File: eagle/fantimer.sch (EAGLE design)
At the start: 17 parts, among them IC1 PIC10F220, K1 PB2032-ND, Q1 2N7000-G, U1 IRM-01-5, X1 732-10957-ND

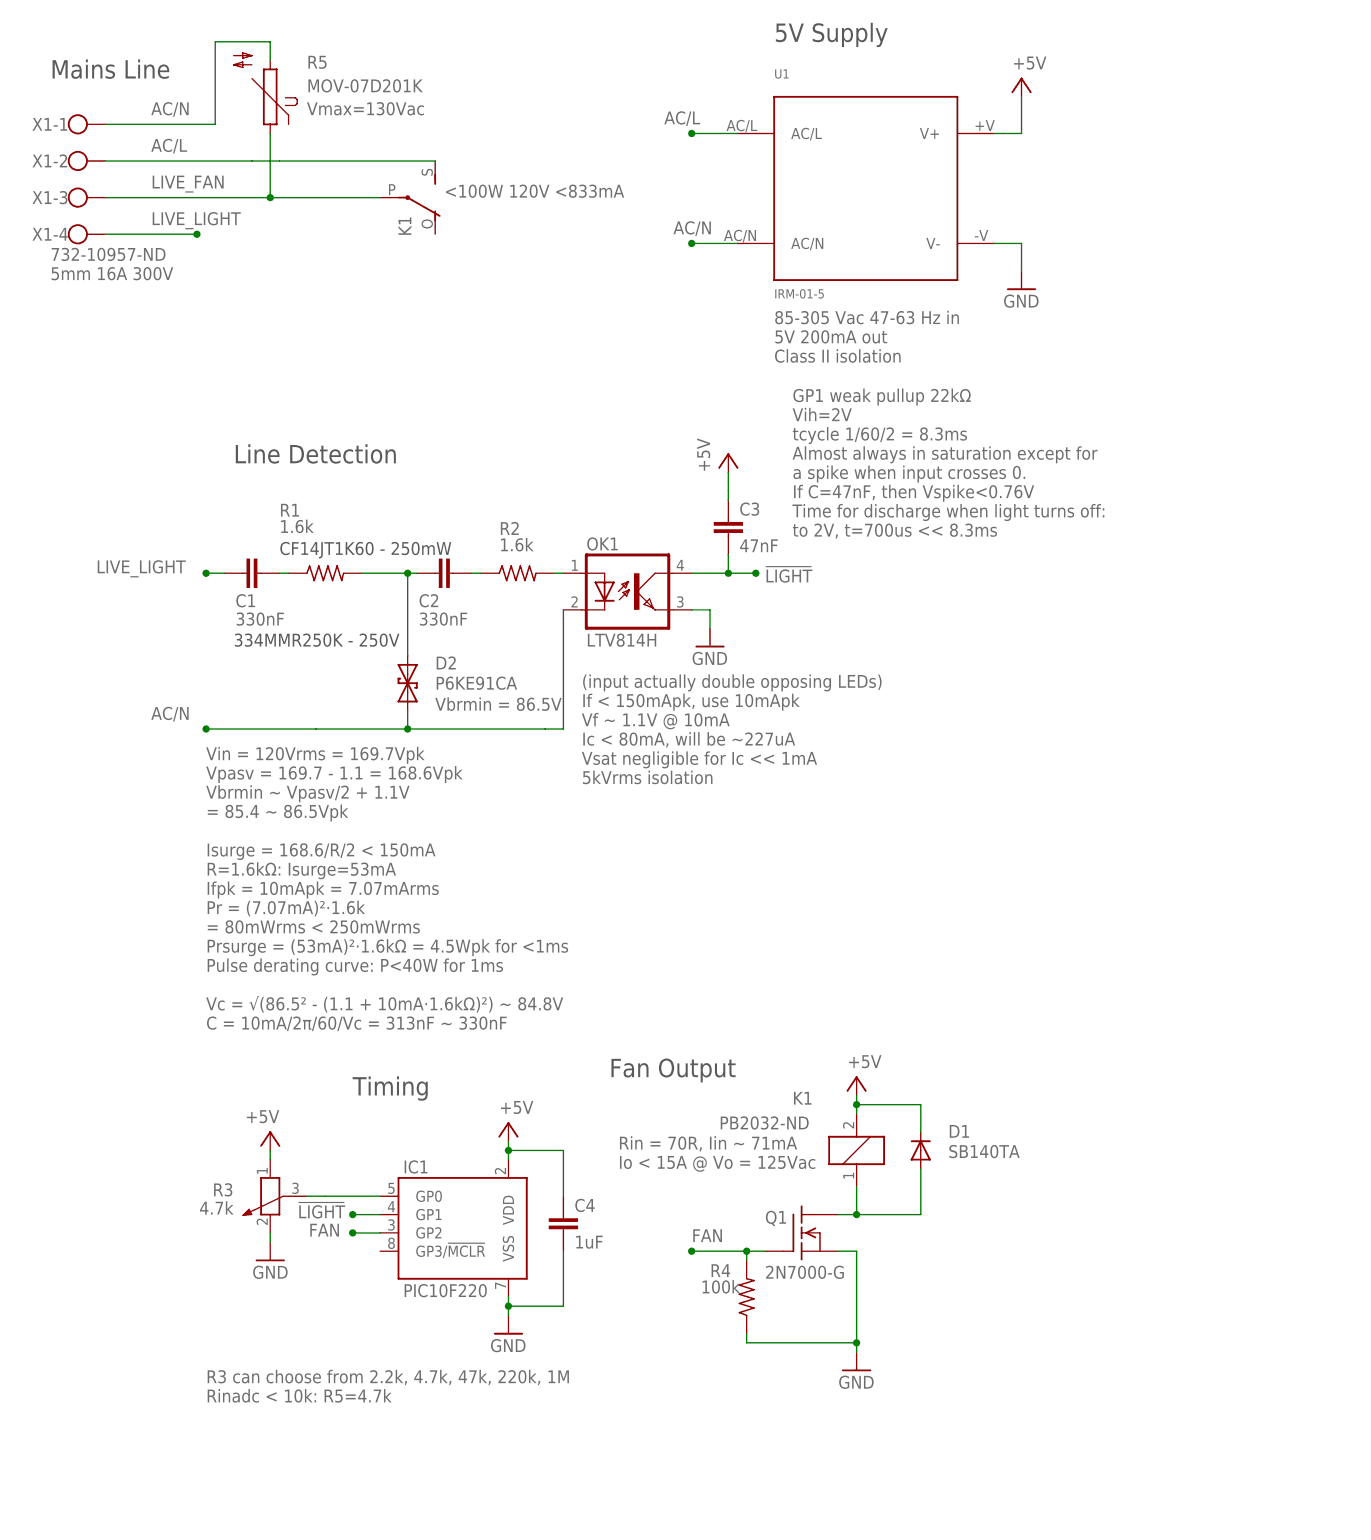
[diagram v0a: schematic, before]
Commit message: Increase detection filter cap; add pot cap
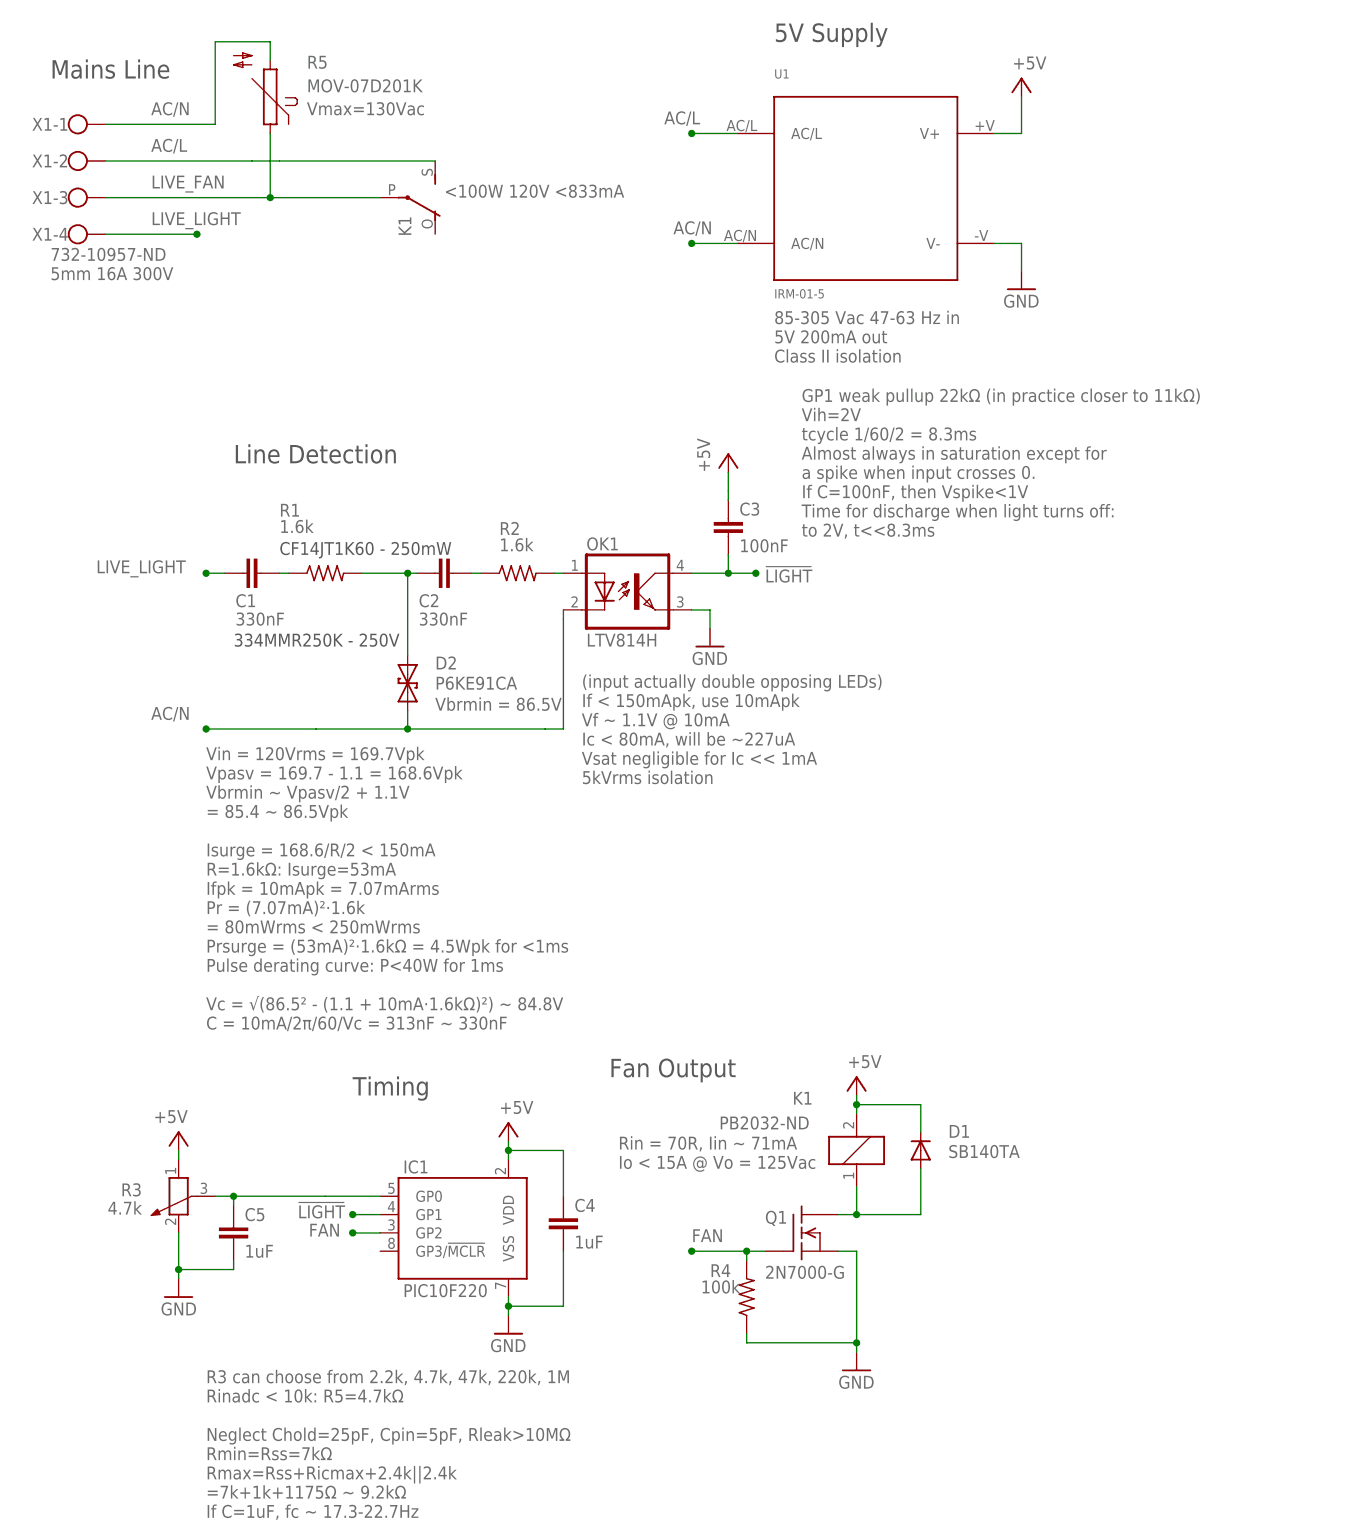
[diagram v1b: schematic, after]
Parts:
- added C5: 1uF, rcl:C-EU025-025X050
- C3: value 47nF -> 100nF
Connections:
- net ADJ: now also C5.1
- net GND: now also C5.2
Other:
- note added: "GP1 weak pullup 22kΩ (in practice closer to 11kΩ) Vih=2V tcycle 1/60/2 = 8.3ms Almost always in saturation except for a spike when input crosses 0. If C=100nF, then Vspike<1V Time for discharge when light turns off: to 2V, t<<8.3ms"
- note added: "R3 can choose from 2.2k, 4.7k, 47k, 220k, 1M Rinadc < 10k: R5=4.7kΩ Neglect Chold=25pF, Cpin=5pF, Rleak>10MΩ Rmin=Rss=7kΩ Rmax=Rss+Ricmax+2.4k||2.4k =7k+1k+1175Ω ~ 9.2kΩ If C=1uF, fc ~ 17.3-22.7Hz"
- note removed: "GP1 weak pullup 22kΩ Vih=2V tcycle 1/60/2 = 8.3ms Almost always in saturation except for a spike when input crosses 0. If C=47nF, then Vspike<0.76V Time for discharge when light turns off: to 2V, t=700us << 8.3ms"
- note removed: "R3 can choose from 2.2k, 4.7k, 47k, 220k, 1M Rinadc < 10k: R5=4.7k"
- moved on the sheet: R3
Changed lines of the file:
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@@
 <part name="P+6" library="supply1" library_urn="urn:adsk.eagle:library:371" deviceset="+5V" device=""/>
 <part name="GND5" library="supply1" library_urn="urn:adsk.eagle:library:371" deviceset="GND" device=""/>
-<part name="C3" library="rcl" library_urn="urn:adsk.eagle:library:334" deviceset="C-EU" device="025-025X050" package3d_urn="urn:adsk.eagle:package:23629/2" value="47nF"/>
+<part name="C3" library="rcl" library_urn="urn:adsk.eagle:library:334" deviceset="C-EU" device="025-025X050" package3d_urn="urn:adsk.eagle:package:23629/2" value="100nF"/>
 <part name="P+2" library="supply1" library_urn="urn:adsk.eagle:library:371" deviceset="+5V" device=""/>
 <part name="IC1" library="microchip-addl" deviceset="PIC10F220" device="-I/P" package3d_urn="urn:adsk.eagle:package:14440/1" value="PIC10F220"/>
@@
 <part name="C4" library="rcl" library_urn="urn:adsk.eagle:library:334" deviceset="C-EU" device="025-025X050" package3d_urn="urn:adsk.eagle:package:23629/2" value="1uF"/>
 <part name="R5" library="varistor" library_urn="urn:adsk.eagle:library:410" deviceset="S05K300" device="" package3d_urn="urn:adsk.eagle:package:30536/1" value="MOV-07D201K"/>
+<part name="C5" library="rcl" library_urn="urn:adsk.eagle:library:334" deviceset="C-EU" device="025-025X050" package3d_urn="urn:adsk.eagle:package:23629/2" value="1uF"/>
 </parts>
 <sheets>
@@
 <text x="-13.97" y="172.72" size="1.778" layer="96">5mm 16A 300V</text>
 <text x="7.62" y="21.59" size="1.778" layer="96" rot="MR180">R3 can choose from 2.2k, 4.7k, 47k, 220k, 1M
-Rinadc &lt; 10k: R5=4.7k</text>
+Rinadc &lt; 10k: R5=4.7kΩ
+Neglect Chold=25pF, Cpin=5pF, Rleak&gt;10MΩ
+Rmin=Rss=7kΩ
+Rmax=Rss+Ricmax+2.4k||2.4k
+=7k+1k+1175Ω ~ 9.2kΩ
+If C=1uF, fc ~ 17.3-22.7Hz</text>
 <text x="86.36" y="161.29" size="1.778" layer="96">85-305 Vac 47-63 Hz in
 5V 200mA out
@@
 C = 10mA/2π/60/Vc = 313nF ~ 330nF</text>
 <text x="39.37" y="113.03" size="1.778" layer="96">Vbrmin = 86.5V</text>
-<text x="88.9" y="137.16" size="1.778" layer="96">GP1 weak pullup 22kΩ
+<text x="90.17" y="137.16" size="1.778" layer="96">GP1 weak pullup 22kΩ (in practice closer to 11kΩ)
 Vih=2V
 tcycle 1/60/2 = 8.3ms
 Almost always in saturation except for
 a spike when input crosses 0.
-If C=47nF, then Vspike&lt;0.76V
+If C=100nF, then Vspike&lt;1V
 Time for discharge when light turns off:
-to 2V, t=700us &lt;&lt; 8.3ms</text>
+to 2V, t&lt;&lt;8.3ms</text>
 <text x="17.78" y="134.62" size="1.778" layer="97">CF14JT1K60‎ - 250mW</text>
 <text x="11.43" y="121.92" size="1.778" layer="97">334MMR250K‎ - 250V</text>
@@
 <attribute name="VALUE" x="17.78" y="137.668" size="1.778" layer="96"/>
 </instance>
-<instance part="R3" gate="1" x="16.51" y="45.72" smashed="yes" rot="MR270">
-<attribute name="NAME" x="11.43" y="45.72" size="1.778" layer="95" rot="MR0"/>
-<attribute name="VALUE" x="11.43" y="43.18" size="1.778" layer="96" rot="MR0"/>
+<instance part="R3" gate="1" x="3.81" y="45.72" smashed="yes" rot="MR270">
+<attribute name="NAME" x="-1.27" y="45.72" size="1.778" layer="95" rot="MR0"/>
+<attribute name="VALUE" x="-1.27" y="43.18" size="1.778" layer="96" rot="MR0"/>
 </instance>
 <instance part="P+6" gate="1" x="49.53" y="55.88" smashed="yes">
 <attribute name="VALUE" x="48.26" y="57.15" size="1.778" layer="96"/>
 </instance>
-<instance part="GND5" gate="1" x="16.51" y="36.83" rot="MR0"/>
+<instance part="GND5" gate="1" x="3.81" y="31.75" rot="MR0"/>
 <instance part="C3" gate="G$1" x="80.01" y="139.7"/>
-<instance part="P+2" gate="1" x="16.51" y="54.61" smashed="yes" rot="MR0">
-<attribute name="VALUE" x="17.78" y="55.88" size="1.778" layer="96" rot="MR0"/>
+<instance part="P+2" gate="1" x="3.81" y="54.61" smashed="yes" rot="MR0">
+<attribute name="VALUE" x="5.08" y="55.88" size="1.778" layer="96" rot="MR0"/>
 </instance>
 <instance part="IC1" gate="G$1" x="43.18" y="41.91"/>
@@
 <attribute name="VALUE" x="21.59" y="198.755" size="1.778" layer="96"/>
 </instance>
+<instance part="C5" gate="G$1" x="11.43" y="41.91"/>
 </instances>
 <busses>
@@
 <segment>
 <pinref part="GND5" gate="1" pin="GND"/>
-<wire x1="16.51" y1="39.37" x2="16.51" y2="40.64" width="0.1524" layer="91"/>
+<wire x1="3.81" y1="34.29" x2="3.81" y2="35.56" width="0.1524" layer="91"/>
 <pinref part="R3" gate="1" pin="2"/>
+<pinref part="C5" gate="G$1" pin="2"/>
+<wire x1="3.81" y1="35.56" x2="3.81" y2="40.64" width="0.1524" layer="91"/>
+<wire x1="11.43" y1="36.83" x2="11.43" y2="35.56" width="0.1524" layer="91"/>
+<wire x1="11.43" y1="35.56" x2="3.81" y2="35.56" width="0.1524" layer="91"/>
+<junction x="3.81" y="35.56"/>
 </segment>
 <segment>
@@
 <pinref part="R3" gate="1" pin="1"/>
 <pinref part="P+2" gate="1" pin="+5V"/>
-<wire x1="16.51" y1="50.8" x2="16.51" y2="52.07" width="0.1524" layer="91"/>
+<wire x1="3.81" y1="50.8" x2="3.81" y2="52.07" width="0.1524" layer="91"/>
 </segment>
 <segment>
@@
 <segment>
 <pinref part="R3" gate="1" pin="3"/>
-<wire x1="21.59" y1="45.72" x2="24.13" y2="45.72" width="0.1524" layer="91"/>
+<wire x1="8.89" y1="45.72" x2="11.43" y2="45.72" width="0.1524" layer="91"/>
 <pinref part="IC1" gate="G$1" pin="GP0"/>
+<wire x1="11.43" y1="45.72" x2="24.13" y2="45.72" width="0.1524" layer="91"/>
 <wire x1="24.13" y1="45.72" x2="31.75" y2="45.72" width="0.1524" layer="91"/>
-</segment>
-</net>
+<pinref part="C5" gate="G$1" pin="1"/>
+<wire x1="11.43" y1="44.45" x2="11.43" y2="45.72" width="0.1524" layer="91"/>
+<junction x="11.43" y="45.72"/>
+</segment>
+</net>
